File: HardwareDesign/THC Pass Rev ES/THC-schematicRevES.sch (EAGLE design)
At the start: 53 parts, among them J1 2.1MM-PLUG-PCB-MNT, J2 DB9-MALE, J3 DB9-FEMALE, Q1 2N2222A, U1 7805T

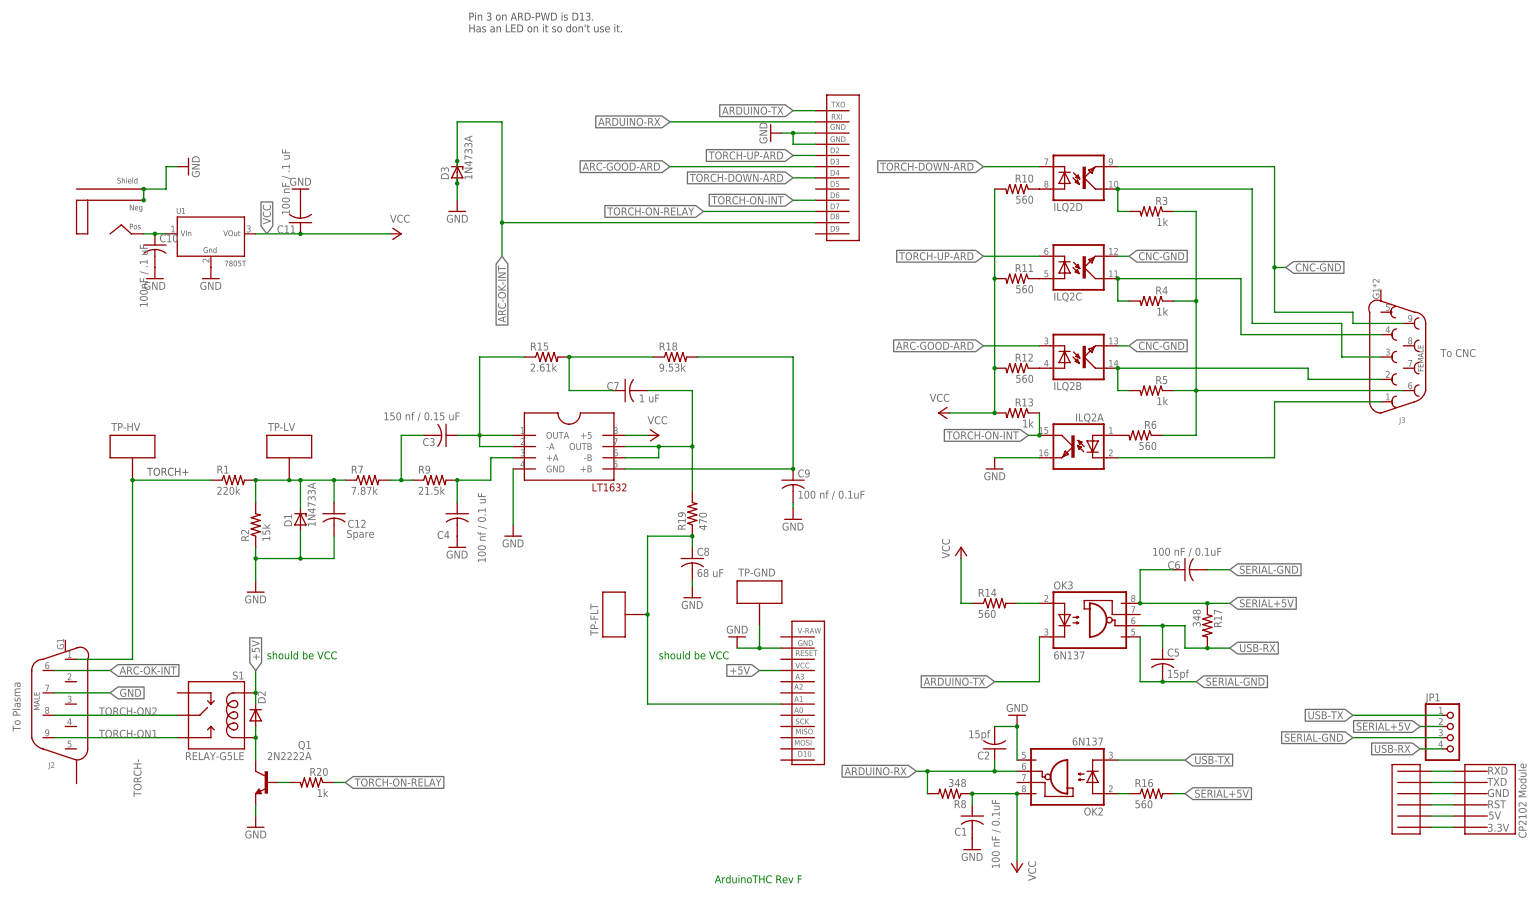
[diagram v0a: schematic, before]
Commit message: Added section to manual for programming the Arduino.  Cleaned up schematic files.
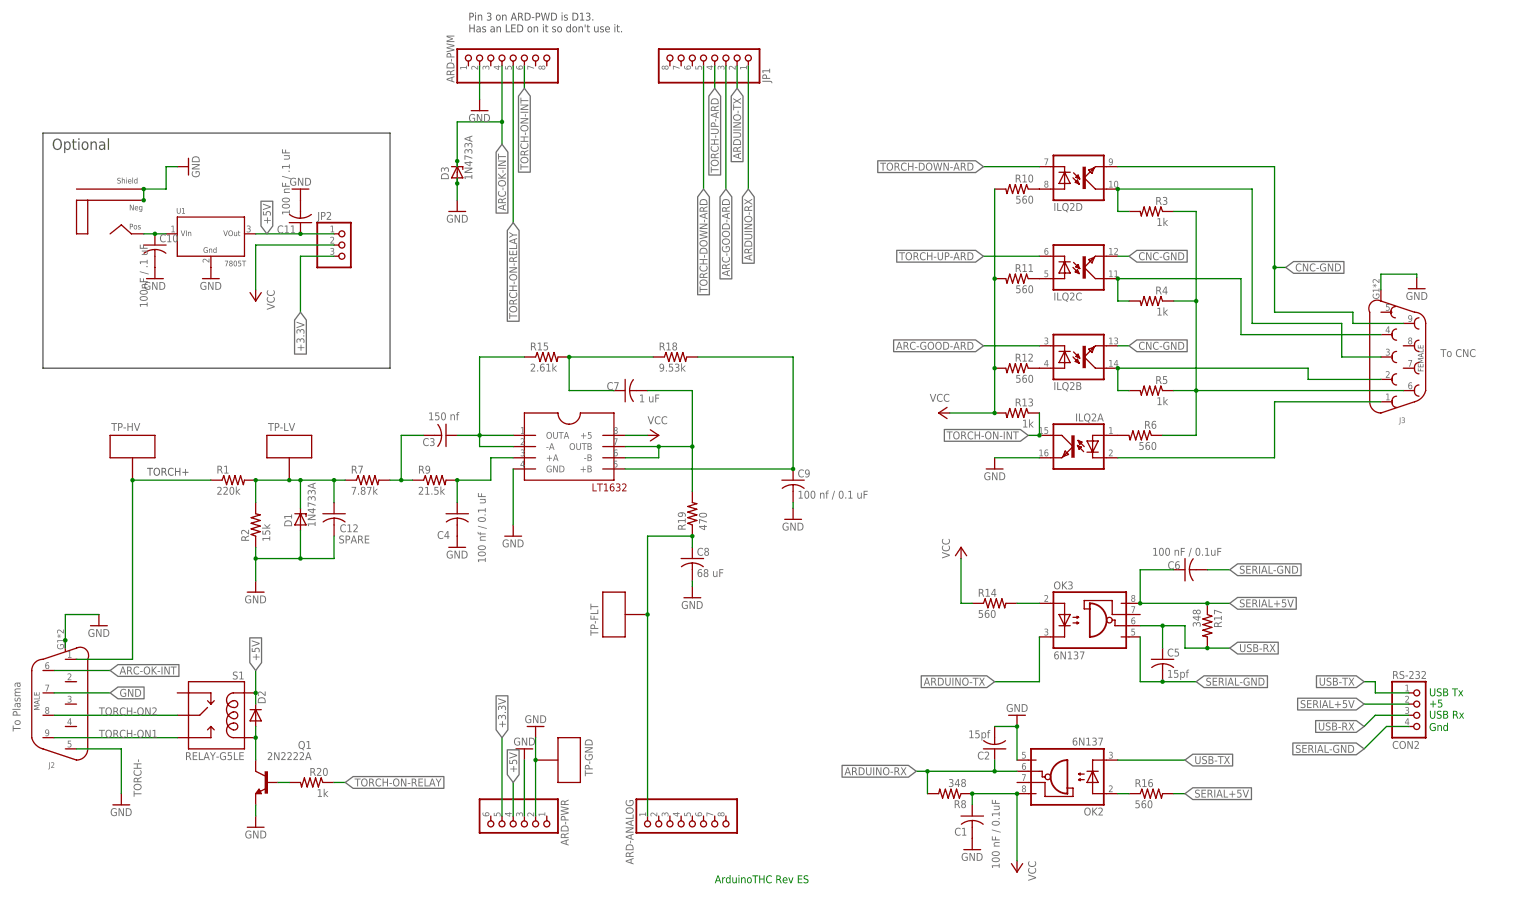
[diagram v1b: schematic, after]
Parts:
- removed MOD1: ARDUINO-PRO-MICRO-FOOTPRINT, ArduinoProMicro:ARDUINO-PRO-MICRO-FOOTPRINT
- removed U$2: CP2102-TTL-USB, CP2102 TTL to USB:CP2102-TTL-USB
- removed U$3: CP2102-PADS, CP2102 TTL to USB:CP2102-PADS
- added ARD-ANALOG, ARD-PWM: (no value), pinhead:PINHD-1X8
- added ARD-PWR: (no value), pinhead:PINHD-1X6
- added JP2: (no value), pinhead:PINHD-1X3
- added RS-232: CON2, pinhead:PINHD-1X4
- C12: value Spare -> SPARE
- C3: value 150 nf / 0.15 uF -> 150 nf
- C9: value 100 nf / 0.1uF -> 100 nf / 0.1 uF
- JP1: device pinhead:PINHD-1X4 -> pinhead:PINHD-1X8
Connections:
- removed net N$10: U$2.P$RST, U$3.P$RST
- removed net N$11: U$2.P$TXD, U$3.P$TXD
- removed net N$12: U$2.P$RXD, U$3.P$RXD
- removed net N$13: U$2.P$GND, U$3.P$GND
- removed net N$14: U$2.P$5V, U$3.P$5V
- removed net N$6: U$2.P$3.3V, U$3.P$3.3V
- new net +3.3V: ARD-PWR.5, JP2.3
- net +5V: now also ARD-PWR.4, C11.1, JP2.1, U1.VOUT; no longer MOD1G$1.VCC
- net ARC-GOOD-ARD: now also JP1.3; no longer MOD1G$2.D3
- net ARC-OK-INT: now also ARD-PWM.4; no longer MOD1G$2.D8
- net ARD-ANALOG-IN: now also ARD-ANALOG.1; no longer MOD1G$1.A1
- net ARDUINO-RX: now also JP1.1; no longer MOD1G$2.RXI
- net ARDUINO-TX: now also JP1.2; no longer MOD1G$2.TX0
- net GND: now also ARD-PWM.2, ARD-PWR.2, ARD-PWR.3, J2.P$5, J2.P$SHLD, J3.P$SHLD; no longer MOD1G$1.GND2, MOD1G$2.GND10, MOD1G$2.GND9
- net SERIAL+5V: now also RS-232.2; no longer JP1.2
- net SERIAL-GND: now also RS-232.4; no longer JP1.3
- net TORCH-DOWN-ARD: now also JP1.5; no longer MOD1G$2.D4
- net TORCH-ON-INT: now also ARD-PWM.6; no longer MOD1G$2.D6
- net TORCH-ON-RELAY: now also ARD-PWM.5; no longer MOD1G$2.D7
- net TORCH-UP-ARD: now also JP1.4; no longer MOD1G$2.D2
- net USB-RX: now also RS-232.3; no longer JP1.4
- net USB-TX: now also RS-232.1; no longer JP1.1
- net VCC: now also JP2.2; no longer C11.1, U1.VOUT
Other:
- note added: "+5"
- note added: "ArduinoTHC Rev ES"
- note added: "Gnd"
- note added: "Optional"
- note added: "USB Rx"
- note added: "USB Tx"
- note removed: "ArduinoTHC Rev F"
- note removed: "should be VCC"
- moved on the sheet: TP-GND
